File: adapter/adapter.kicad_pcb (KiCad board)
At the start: 2 copper layers, 93.5 x 50.9 mm, 22 parts, among them J10 Ribbon, J11 Ribbon, J12 Ribbon, J3 Battery charge, J6 Battery charge, J7 Trackball, J8 Trackball, J9 Ribbon, SW1 SW_SPST, SW2 SW_SPST, SW3 SW_SPDT, SW4 SW_SPDT, U1 eliteC, U2 eliteC

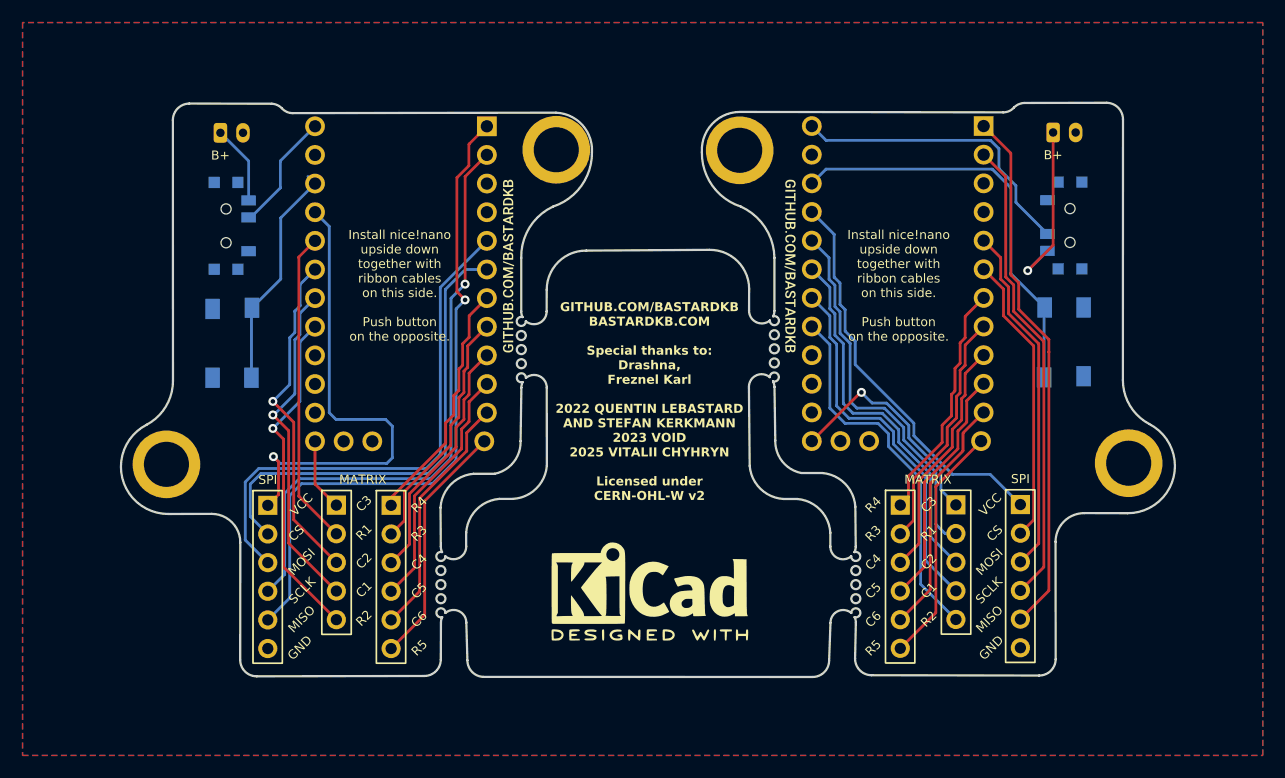
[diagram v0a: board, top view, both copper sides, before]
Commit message: Move back the power switch and reset button
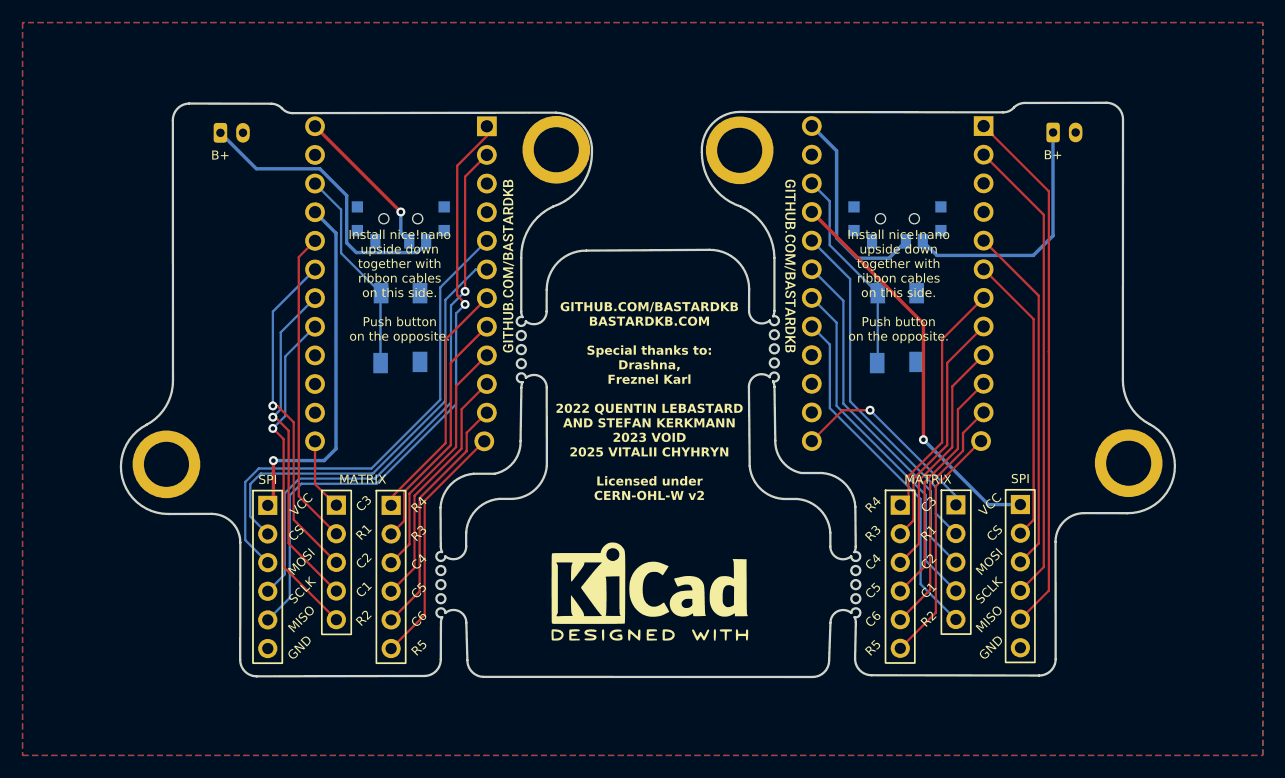
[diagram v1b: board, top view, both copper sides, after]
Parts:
- moved SW3 15.5 mm to (133.5, 77.4), turned to 0 degrees
- moved SW4 15.3 mm to (177.6, 77.4), turned to 0 degrees
- moved SW1 15.1 mm to (133.6, 87.1), turned to -90 degrees
- moved SW2 14.9 mm to (177.6, 87.1)
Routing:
- net Rst2: track 37.0 -> 18.4 mm
- net bat_sw_l: track 7.04 -> 25.6 mm
- net +5V_1: track 43.6 -> 32.4 mm
- net bat_r: track 26.8 -> 18.4 mm
- net bat_sw_r: track 15.8 -> 21.9 mm, vias 1 -> 0
- net ss_l: track 42.6 -> 39.2 mm
- net miso_l: track 59.2 -> 56.3 mm
- net sc_l: track 53.6 -> 50.7 mm
- net mosi_l: track 46.9 -> 44.1 mm
- net col3_r: track 20.4 -> 17.9 mm
- net bat_l: track 11.3 -> 13.7 mm, vias 0 -> 1
- net Rst: track 20.4 -> 18.4 mm
- net row1_r: track 33.3 -> 31.3 mm
- net row2_r: track 33.0 -> 31.3 mm
- net col1_r: track 32.9 -> 31.3 mm
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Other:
- board text added: "ON / OFF"
- board text removed: "OFF / ON"
